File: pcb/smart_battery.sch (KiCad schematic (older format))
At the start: 39 parts, among them J1 feather long, J10 feather short, J11 Conn_01x05_RTC, J12 Conn_HtrTh, J13 Conn_BattTh, J2 feather short, J3 feather long, J4 feather short, J5 feather long, J6 feather short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

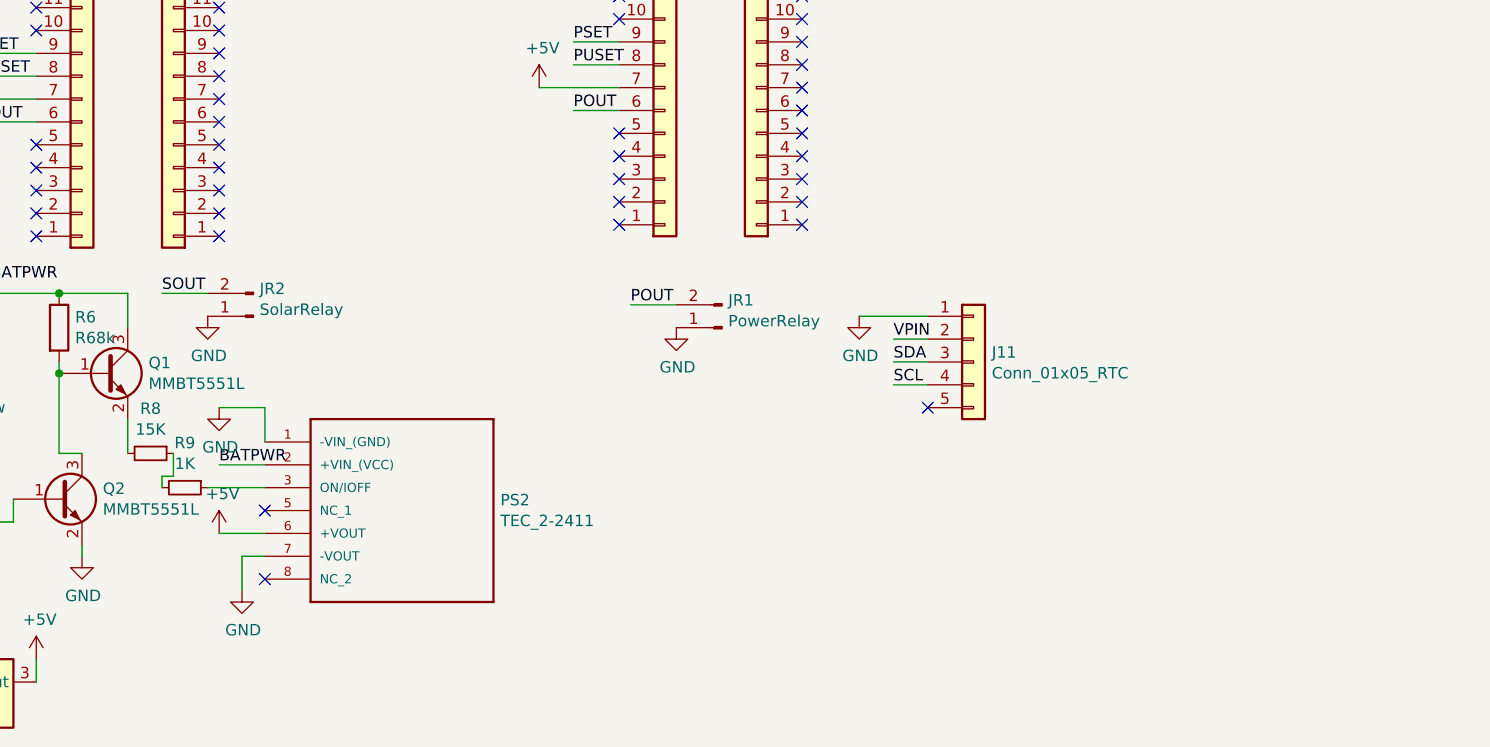
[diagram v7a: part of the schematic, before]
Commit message: Added i2c connector
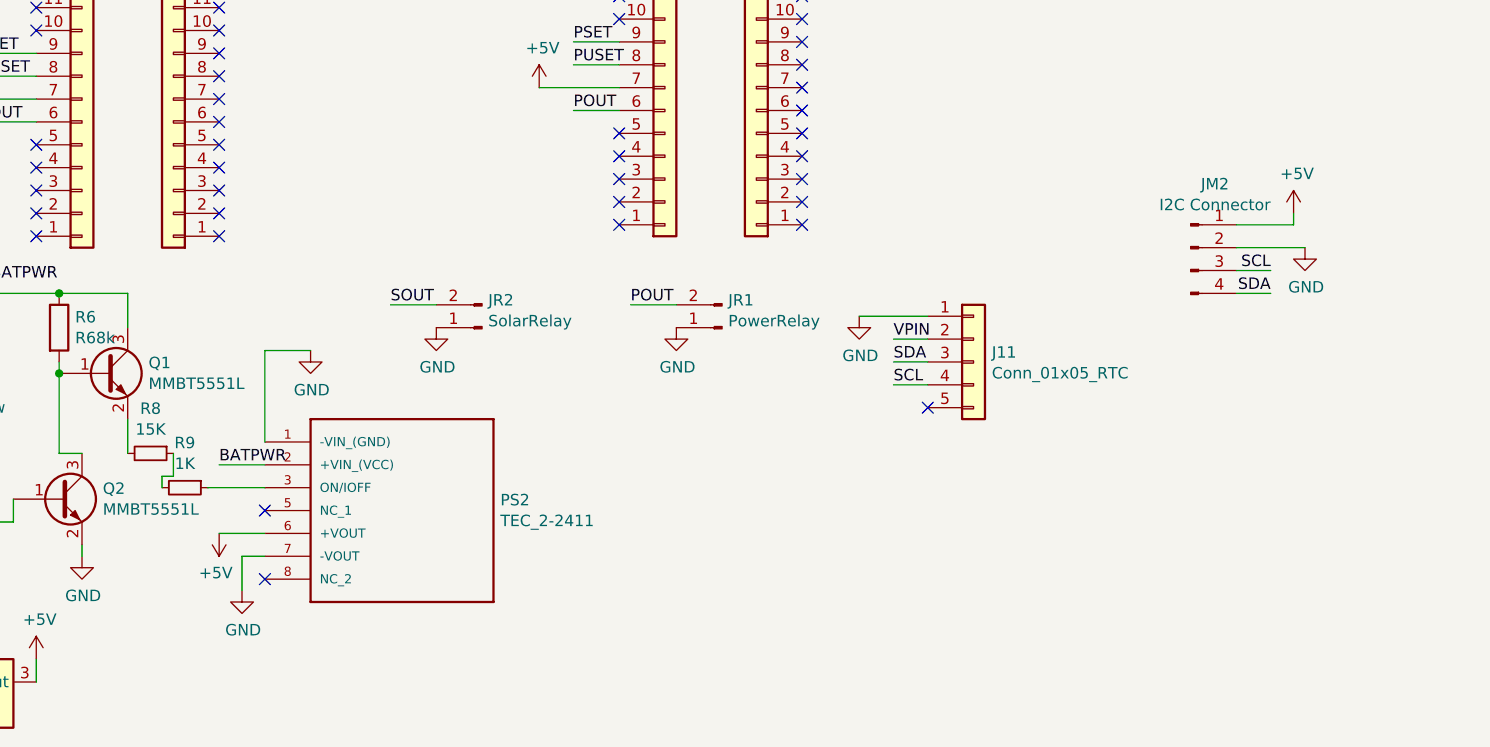
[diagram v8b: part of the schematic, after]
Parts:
- added JM2: I2C Connector, symbol Connector:Conn_01x04_Male
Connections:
- net +5V: now also JM2.1 (Pin_1)
- net GND: now also JM2.2 (Pin_2)
- net SCL: now also JM2.3 (Pin_3)
- net SDA: now also JM2.4 (Pin_4)
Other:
- moved on the sheet: JR2
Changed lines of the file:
@@
 L Connector:Conn_01x02_Male JR2
 U 1 1 60168A13
-P 4950 5450
-F 0 "JR2" H 4923 5330 50  0000 R CNN
-F 1 "SolarRelay" H 4923 5421 50  0000 R CNN
-F 2 "" H 4950 5450 50  0001 C CNN
-F 3 "~" H 4950 5450 50  0001 C CNN
-	1    4950 5450
+P 5950 5500
+F 0 "JR2" H 5923 5380 50  0000 R CNN
+F 1 "SolarRelay" H 5923 5471 50  0000 R CNN
+F 2 "" H 5950 5500 50  0001 C CNN
+F 3 "~" H 5950 5500 50  0001 C CNN
+	1    5950 5500
 	-1   0    0    1
 $EndComp
@@
 L power:GND #PWR021
 U 1 1 60168CFD
-P 4750 5450
-F 0 "#PWR021" H 4750 5200 50  0001 C CNN
-F 1 "GND" H 4755 5277 50  0000 C CNN
-F 2 "" H 4750 5450 50  0001 C CNN
-F 3 "" H 4750 5450 50  0001 C CNN
-	1    4750 5450
-	1    0    0    -1
-$EndComp
-Text Label 4550 5350 0    50   ~ 0
+P 5750 5500
+F 0 "#PWR021" H 5750 5250 50  0001 C CNN
+F 1 "GND" H 5755 5327 50  0000 C CNN
+F 2 "" H 5750 5500 50  0001 C CNN
+F 3 "" H 5750 5500 50  0001 C CNN
+	1    5750 5500
+	1    0    0    -1
+$EndComp
+Text Label 5550 5400 0    50   ~ 0
 SOUT
 Wire Wire Line
-	4550 5350 4750 5350
+	5550 5400 5750 5400
 $Comp
 L Connector:Conn_01x02_Male JR1
@@
 L power:GND #PWR022
 U 1 1 601D774F
-P 4800 5850
-F 0 "#PWR022" H 4800 5600 50  0001 C CNN
-F 1 "GND" H 4805 5677 50  0000 C CNN
-F 2 "" H 4800 5850 50  0001 C CNN
-F 3 "" H 4800 5850 50  0001 C CNN
-	1    4800 5850
+P 5200 5600
+F 0 "#PWR022" H 5200 5350 50  0001 C CNN
+F 1 "GND" H 5205 5427 50  0000 C CNN
+F 2 "" H 5200 5600 50  0001 C CNN
+F 3 "" H 5200 5600 50  0001 C CNN
+	1    5200 5600
 	1    0    0    -1
 $EndComp
@@
 F 3 "" H 4800 6400 50  0001 C CNN
 	1    4800 6400
-	1    0    0    -1
+	-1   0    0    1
 $EndComp
 Wire Wire Line
@@
 	1    0    0    -1
 $EndComp
-Wire Wire Line
-	5000 5850 5000 6000
-Wire Wire Line
-	4800 5850 5000 5850
 Text Label 3800 5300 0    50   ~ 0
 BATPWR
@@
 Connection ~ 4100 5350
 $Comp
+L power:+5V #PWR?
+U 1 1 601F6B4D
+P 3250 2450
+F 0 "#PWR?" H 3250 2300 50  0001 C CNN
+F 1 "+5V" H 3265 2623 50  0000 C CNN
+F 2 "" H 3250 2450 50  0001 C CNN
+F 3 "" H 3250 2450 50  0001 C CNN
+	1    3250 2450
+	1    0    0    -1
+$EndComp
+Wire Wire Line
+	3100 2650 3250 2650
+Wire Wire Line
+	3250 2650 3250 2450
+$Comp
+L power:GND #PWR?
+U 1 1 602008F6
+P 3300 2750
+F 0 "#PWR?" H 3300 2500 50  0001 C CNN
+F 1 "GND" H 3305 2577 50  0000 C CNN
+F 2 "" H 3300 2750 50  0001 C CNN
+F 3 "" H 3300 2750 50  0001 C CNN
+	1    3300 2750
+	1    0    0    -1
+$EndComp
+Wire Wire Line
+	3100 2750 3300 2750
+Text Label 3150 2850 0    50   ~ 0
+RX
+Text Label 3150 2950 0    50   ~ 0
+TX
+Wire Wire Line
+	3100 2850 3150 2850
+Wire Wire Line
+	3100 2950 3150 2950
+$Comp
 L Connector:Conn_01x04_Male JM1
 U 1 1 601F67BE
@@
 $EndComp
 $Comp
+L Connector:Conn_01x04_Male JM2
+U 1 1 6021EF56
+P 9050 5150
+F 0 "JM2" H 9156 5428 50  0000 C CNN
+F 1 "I2C Connector" H 9156 5337 50  0000 C CNN
+F 2 "" H 9050 5150 50  0001 C CNN
+F 3 "~" H 9050 5150 50  0001 C CNN
+	1    9050 5150
+	1    0    0    -1
+$EndComp
+$Comp
 L power:+5V #PWR?
-U 1 1 601F6B4D
-P 3250 2450
-F 0 "#PWR?" H 3250 2300 50  0001 C CNN
-F 1 "+5V" H 3265 2623 50  0000 C CNN
-F 2 "" H 3250 2450 50  0001 C CNN
-F 3 "" H 3250 2450 50  0001 C CNN
-	1    3250 2450
-	1    0    0    -1
-$EndComp
-Wire Wire Line
-	3100 2650 3250 2650
-Wire Wire Line
-	3250 2650 3250 2450
+U 1 1 60229670
+P 9500 5000
+F 0 "#PWR?" H 9500 4850 50  0001 C CNN
+F 1 "+5V" H 9515 5173 50  0000 C CNN
+F 2 "" H 9500 5000 50  0001 C CNN
+F 3 "" H 9500 5000 50  0001 C CNN
+	1    9500 5000
+	1    0    0    -1
+$EndComp
+Wire Wire Line
+	9250 5050 9500 5050
+Wire Wire Line
+	9500 5050 9500 5000
 $Comp
 L power:GND #PWR?
-U 1 1 602008F6
-P 3300 2750
-F 0 "#PWR?" H 3300 2500 50  0001 C CNN
-F 1 "GND" H 3305 2577 50  0000 C CNN
-F 2 "" H 3300 2750 50  0001 C CNN
-F 3 "" H 3300 2750 50  0001 C CNN
-	1    3300 2750
-	1    0    0    -1
-$EndComp
-Wire Wire Line
-	3100 2750 3300 2750
-Text Label 3150 2850 0    50   ~ 0
-RX
-Text Label 3150 2950 0    50   ~ 0
-TX
-Wire Wire Line
-	3100 2850 3150 2850
-Wire Wire Line
-	3100 2950 3150 2950
+U 1 1 60233C1C
+P 9550 5150
+F 0 "#PWR?" H 9550 4900 50  0001 C CNN
+F 1 "GND" H 9555 4977 50  0000 C CNN
+F 2 "" H 9550 5150 50  0001 C CNN
+F 3 "" H 9550 5150 50  0001 C CNN
+	1    9550 5150
+	1    0    0    -1
+$EndComp
+Wire Wire Line
+	9250 5150 9550 5150
+Text Label 9400 5250 2    50   ~ 0
+SCL
+Text Label 9400 5350 2    50   ~ 0
+SDA
+Wire Wire Line
+	9250 5350 9400 5350
+Wire Wire Line
+	9250 5250 9400 5250
+Wire Wire Line
+	5200 5600 5000 5600
+Wire Wire Line
+	5000 5600 5000 6000
 $EndSCHEMATC
